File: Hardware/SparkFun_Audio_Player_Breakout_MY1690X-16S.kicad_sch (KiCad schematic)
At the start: 42 parts, among them J1 3.5mm TRRS, J2 Conn_01x03, J3 Conn_01x02, J4 USB_C_Receptacle, J5 Conn_01x06, J6 microSD, Q1 BSS138, U2 MY1690X-16S

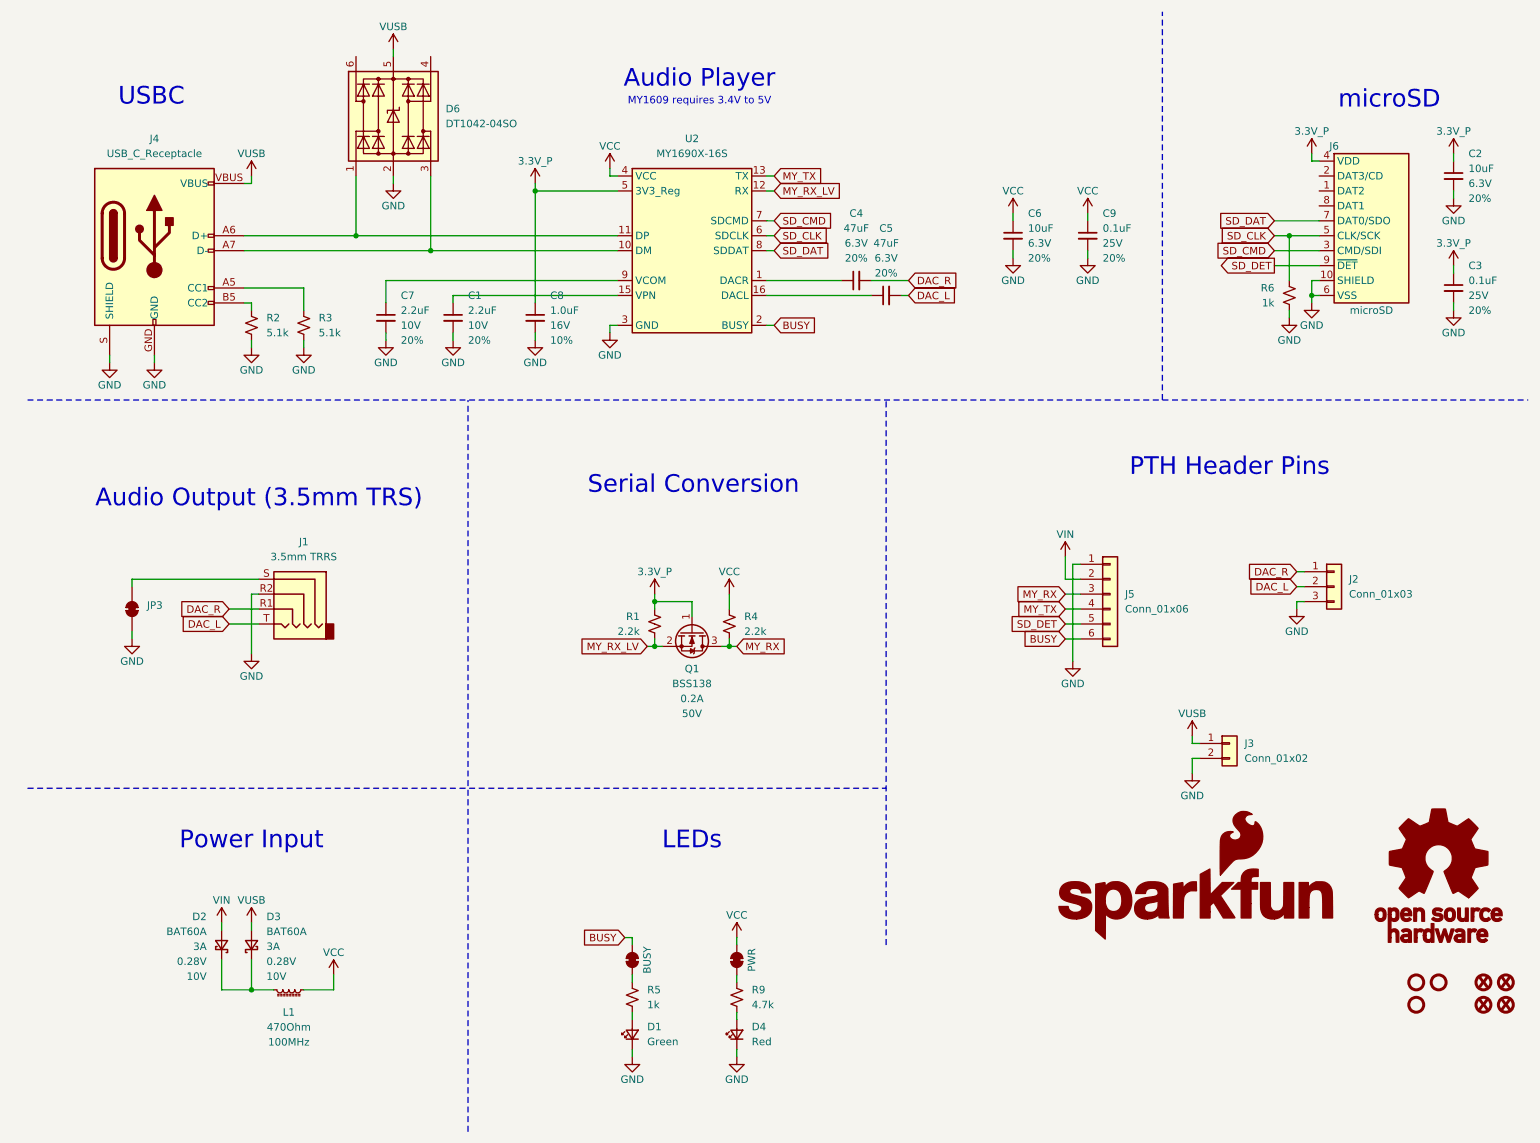
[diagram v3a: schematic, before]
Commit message: review changes 1
-TX bottom silk fishtail (output)
-centered position of OSHW logo
-nudged vcc vias near VUSB pth headers for better ground flow pour
-named JP3 "SLV"
-added jumper comments to sch
-moved C1/C8 to avoid text overlap in SCH
-added RD to jumpers in sch
-added NC flags to unused pins on SCH
-measures
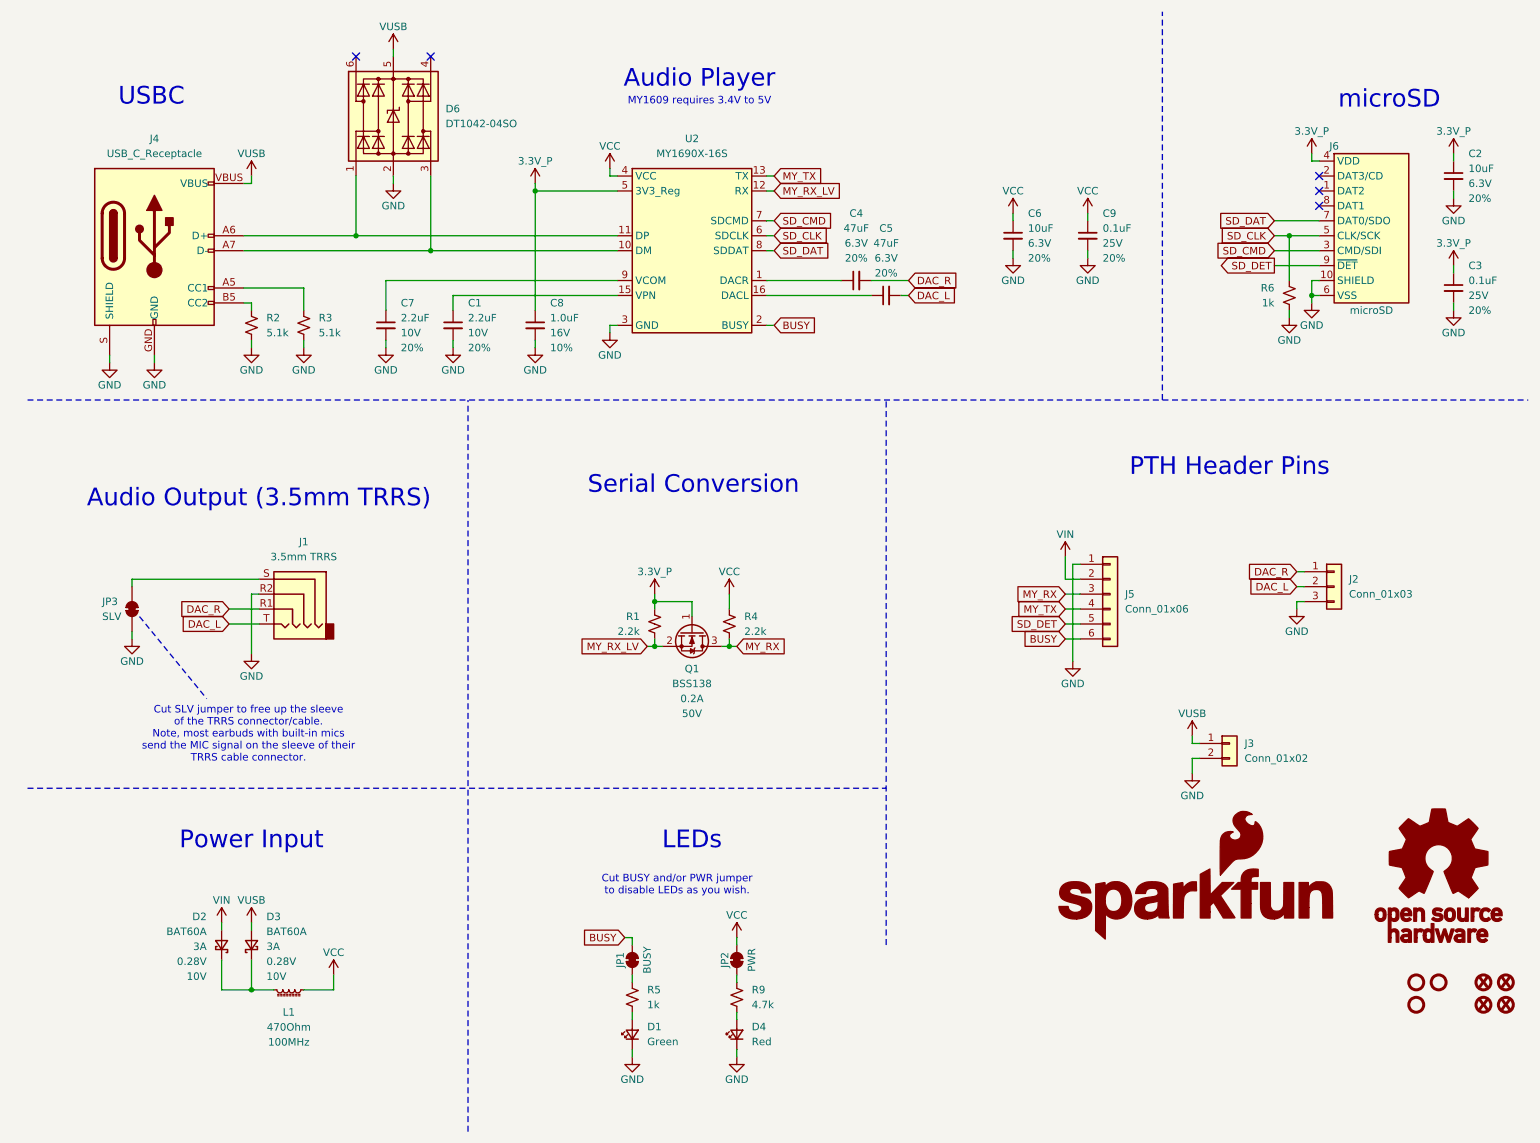
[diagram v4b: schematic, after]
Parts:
- JP3: value ~ -> SLV
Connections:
- no-connect marks 0 -> 5
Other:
- note added: "Audio Output (3.5mm TRRS)"
- note added: "Cut BUSY and/or PWR jumper to disable LEDs as you wish."
- note added: "Cut SLV jumper to free up the sleeve of the TRRS connector/cable. Note, most earbuds with built-in mics send the MIC signal on the sleeve of their TRRS cable connector."
- note removed: "Audio Output (3.5mm TRS)"
- moved on the sheet: C1, C7, C8
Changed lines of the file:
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@@
 		(color 0 0 0 0)
 	)
+	(no_connect
+		(at 81.28 20.32)
+	)
+	(no_connect
+		(at 232.41 40.64)
+	)
+	(no_connect
+		(at 68.58 20.32)
+	)
+	(no_connect
+		(at 232.41 43.18)
+	)
+	(no_connect
+		(at 232.41 45.72)
+	)
 	(wire
 		(pts
@@
 	(wire
 		(pts
-			(xy 73.66 68.58) (xy 73.66 67.31)
+			(xy 73.66 69.85) (xy 73.66 68.58)
 		)
 		(stroke
@@
 	(wire
 		(pts
-			(xy 85.09 60.96) (xy 85.09 62.23)
+			(xy 85.09 60.96) (xy 85.09 63.5)
 		)
 		(stroke
@@
 	(wire
 		(pts
-			(xy 73.66 58.42) (xy 73.66 62.23)
+			(xy 73.66 58.42) (xy 73.66 63.5)
 		)
 		(stroke
@@
 	(polyline
 		(pts
+			(xy 31.75 115.57) (xy 43.18 129.54)
+		)
+		(stroke
+			(width 0)
+			(type dash)
+			(color 132 132 132 1)
+		)
+	)
+	(polyline
+		(pts
 			(xy 12.7 78.74) (xy 137.16 78.74)
 		)
@@
 	(wire
 		(pts
-			(xy 99.06 43.18) (xy 99.06 62.23)
+			(xy 99.06 43.18) (xy 99.06 63.5)
 		)
 		(stroke
@@
 	(wire
 		(pts
-			(xy 85.09 68.58) (xy 85.09 67.31)
+			(xy 85.09 69.85) (xy 85.09 68.58)
 		)
 		(stroke
@@
 	(wire
 		(pts
-			(xy 99.06 68.58) (xy 99.06 67.31)
+			(xy 99.06 69.85) (xy 99.06 68.58)
 		)
 		(stroke
@@
 			(font
 				(size 1.27 1.27)
+				(color 132 132 132 1)
 			)
 		)
@@
 		)
 	)
-	(text "Audio Output (3.5mm TRS)"
+	(text "Audio Output (3.5mm TRRS)"
 		(exclude_from_sim no)
 		(at 52.07 95.504 0)
@@
 		)
 	)
+	(text "Cut BUSY and/or PWR jumper\nto disable LEDs as you wish."
+		(exclude_from_sim no)
+		(at 123.19 161.29 0)
+		(effects
+			(font
+				(size 1.27 1.27)
+				(color 132 132 132 1)
+			)
+		)
+	)
 	(text "USBC"
 		(exclude_from_sim no)
@@
 		)
 	)
+	(text "Cut SLV jumper to free up the sleeve\nof the TRRS connector/cable.\nNote, most earbuds with built-in mics\nsend the MIC signal on the sleeve of their\nTRRS cable connector."
+		(exclude_from_sim no)
+		(at 50.292 135.636 0)
+		(effects
+			(font
+				(size 1.27 1.27)
+				(color 132 132 132 1)
+			)
+		)
+	)
 	(text "Power Input"
 		(exclude_from_sim no)
@@
 	(symbol
 		(lib_id "SparkFun-Capacitor:2.2uF_0603_10V_20%")
-		(at 73.66 64.77 0)
+		(at 73.66 66.04 0)
 		(unit 1)
 		(exclude_from_sim no)
@@
 		(fields_autoplaced yes)
 		(property "Reference" "C7"
-			(at 76.2 60.9662 0)
+			(at 76.2 62.2362 0)
 			(effects
 				(font
@@
 		)
 		(property "Value" "2.2uF"
-			(at 76.2 63.5062 0)
+			(at 76.2 64.7762 0)
 			(effects
 				(font
@@
 		)
 		(property "Footprint" "SparkFun-Capacitor:C_0603_1608Metric"
-			(at 73.66 76.2 0)
+			(at 73.66 77.47 0)
 			(effects
 				(font
@@
 		)
 		(property "Datasheet" "https://cdn.sparkfun.com/assets/8/a/4/a/5/Kemet_Capacitor_Datasheet.pdf"
-			(at 74.93 81.28 0)
+			(at 74.93 82.55 0)
 			(effects
 				(font
@@
 		)
 		(property "Description" "Unpolarized capacitor"
-			(at 73.66 83.82 0)
+			(at 73.66 85.09 0)
 			(effects
 				(font
@@
 		)
 		(property "PROD_ID" "CAP-07888"
-			(at 72.39 78.74 0)
+			(at 72.39 80.01 0)
 			(effects
 				(font
@@
 		)
 		(property "Voltage" "10V"
-			(at 76.2 66.0462 0)
+			(at 76.2 67.3162 0)
 			(effects
 				(font
@@
 		)
 		(property "Tolerance" "20%"
-			(at 76.2 68.5862 0)
+			(at 76.2 69.8562 0)
 			(effects
 				(font
@@
 		(on_board yes)
 		(dnp no)
-		(fields_autoplaced yes)
 		(property "Reference" "JP3"
-			(at 33.02 113.6649 90)
+			(at 25.4 113.03 90)
 			(effects
 				(font
@@
 			)
 		)
-		(property "Value" "~"
-			(at 33.02 115.57 90)
+		(property "Value" "SLV"
+			(at 25.4 115.57 90)
 			(effects
 				(font
@@
 	(symbol
 		(lib_id "SparkFun-Capacitor:2.2uF_0603_10V_20%")
-		(at 85.09 64.77 0)
+		(at 85.09 66.04 0)
 		(unit 1)
 		(exclude_from_sim no)
@@
 		(fields_autoplaced yes)
 		(property "Reference" "C1"
-			(at 87.63 60.9662 0)
+			(at 87.63 62.2362 0)
 			(effects
 				(font
@@
 		)
 		(property "Value" "2.2uF"
-			(at 87.63 63.5062 0)
+			(at 87.63 64.7762 0)
 			(effects
 				(font
@@
 		)
 		(property "Footprint" "SparkFun-Capacitor:C_0603_1608Metric"
-			(at 85.09 76.2 0)
+			(at 85.09 77.47 0)
 			(effects
 				(font
@@
 		)
 		(property "Datasheet" "https://cdn.sparkfun.com/assets/8/a/4/a/5/Kemet_Capacitor_Datasheet.pdf"
-			(at 86.36 81.28 0)
+			(at 86.36 82.55 0)
 			(effects
 				(font
@@
 		)
 		(property "Description" "Unpolarized capacitor"
-			(at 85.09 83.82 0)
+			(at 85.09 85.09 0)
 			(effects
 				(font
@@
 		)
 		(property "PROD_ID" "CAP-07888"
-			(at 83.82 78.74 0)
+			(at 83.82 80.01 0)
 			(effects
 				(font
@@
 		)
 		(property "Voltage" "10V"
-			(at 87.63 66.0462 0)
+			(at 87.63 67.3162 0)
 			(effects
 				(font
@@
 		)
 		(property "Tolerance" "20%"
-			(at 87.63 68.5862 0)
+			(at 87.63 69.8562 0)
 			(effects
 				(font
@@
 	(symbol
 		(lib_id "SparkFun-Capacitor:1.0uF_0603_16V_10%")
-		(at 99.06 64.77 0)
+		(at 99.06 66.04 0)
 		(unit 1)
 		(exclude_from_sim no)
@@
 		(fields_autoplaced yes)
 		(property "Reference" "C8"
-			(at 101.6 60.9662 0)
+			(at 101.6 62.2362 0)
 			(effects
 				(font
@@
 		)
 		(property "Value" "1.0uF"
-			(at 101.6 63.5062 0)
+			(at 101.6 64.7762 0)
 			(effects
 				(font
@@
 		)
 		(property "Footprint" "SparkFun-Capacitor:C_0603_1608Metric"
-			(at 99.06 76.2 0)
+			(at 99.06 77.47 0)
 			(effects
 				(font
@@
 		)
 		(property "Datasheet" "https://cdn.sparkfun.com/assets/8/a/4/a/5/Kemet_Capacitor_Datasheet.pdf"
-			(at 99.06 78.74 0)
+			(at 99.06 80.01 0)
 			(effects
 				(font
@@
 		)
 		(property "Description" "Unpolarized capacitor"
-			(at 99.06 83.82 0)
+			(at 99.06 85.09 0)
 			(effects
 				(font
@@
 		)
 		(property "PROD_ID" "CAP-13930"
-			(at 97.79 81.28 0)
+			(at 97.79 82.55 0)
 			(effects
 				(font
@@
 		)
 		(property "Voltage" "16V"
-			(at 101.6 66.0462 0)
+			(at 101.6 67.3162 0)
 			(effects
 				(font
@@
 		)
 		(property "Tolerance" "10%"
-			(at 101.6 68.5862 0)
+			(at 101.6 69.8562 0)
 			(effects
 				(font
@@
 	(symbol
 		(lib_id "SparkFun-PowerSymbol:GND")
-		(at 85.09 68.58 0)
+		(at 85.09 69.85 0)
 		(unit 1)
 		(exclude_from_sim no)
@@
 		(dnp no)
 		(property "Reference" "#PWR013"
-			(at 85.09 74.93 0)
+			(at 85.09 76.2 0)
 			(effects
 				(font
@@
 		)
 		(property "Value" "GND"
-			(at 85.09 72.39 0)
+			(at 85.09 73.66 0)
 			(effects
 				(font
@@
 		)
 		(property "Footprint" ""
-			(at 85.09 68.58 0)
+			(at 85.09 69.85 0)
 			(effects
 				(font
@@
 		)
 		(property "Datasheet" ""
-			(at 85.09 68.58 0)
+			(at 85.09 69.85 0)
 			(effects
 				(font
@@
 		)
 		(property "Description" "Power symbol creates a global label with name \"GND\" , ground"
-			(at 85.09 68.58 0)
+			(at 85.09 69.85 0)
 			(effects
 				(font
@@
 	(symbol
 		(lib_id "SparkFun-PowerSymbol:GND")
-		(at 99.06 68.58 0)
+		(at 99.06 69.85 0)
 		(unit 1)
 		(exclude_from_sim no)
@@
 		(dnp no)
 		(property "Reference" "#PWR015"
-			(at 99.06 74.93 0)
+			(at 99.06 76.2 0)
 			(effects
 				(font
@@
 		)
 		(property "Value" "GND"
-			(at 99.06 72.39 0)
+			(at 99.06 73.66 0)
 			(effects
 				(font
@@
 		)
 		(property "Footprint" ""
-			(at 99.06 68.58 0)
+			(at 99.06 69.85 0)
 			(effects
 				(font
@@
 		)
 		(property "Datasheet" ""
-			(at 99.06 68.58 0)
+			(at 99.06 69.85 0)
 			(effects
 				(font
@@
 		)
 		(property "Description" "Power symbol creates a global label with name \"GND\" , ground"
-			(at 99.06 68.58 0)
+			(at 99.06 69.85 0)
 			(effects
 				(font
@@
 	(symbol
 		(lib_id "SparkFun-PowerSymbol:GND")
-		(at 73.66 68.58 0)
+		(at 73.66 69.85 0)
 		(unit 1)
 		(exclude_from_sim no)
@@
 		(dnp no)
 		(property "Reference" "#PWR014"
-			(at 73.66 74.93 0)
+			(at 73.66 76.2 0)
 			(effects
 				(font
@@
 		)
 		(property "Value" "GND"
-			(at 73.66 72.39 0)
+			(at 73.66 73.66 0)
 			(effects
 				(font
@@
 		)
 		(property "Footprint" ""
-			(at 73.66 68.58 0)
+			(at 73.66 69.85 0)
 			(effects
 				(font
@@
 		)
 		(property "Datasheet" ""
-			(at 73.66 68.58 0)
+			(at 73.66 69.85 0)
 			(effects
 				(font
@@
 		)
 		(property "Description" "Power symbol creates a global label with name \"GND\" , ground"
-			(at 73.66 68.58 0)
+			(at 73.66 69.85 0)
 			(effects
 				(font
@@
 					(size 1.27 1.27)
 				)
-				(hide yes)
 			)
 		)
@@
 					(size 1.27 1.27)
 				)
-				(hide yes)
 			)
 		)

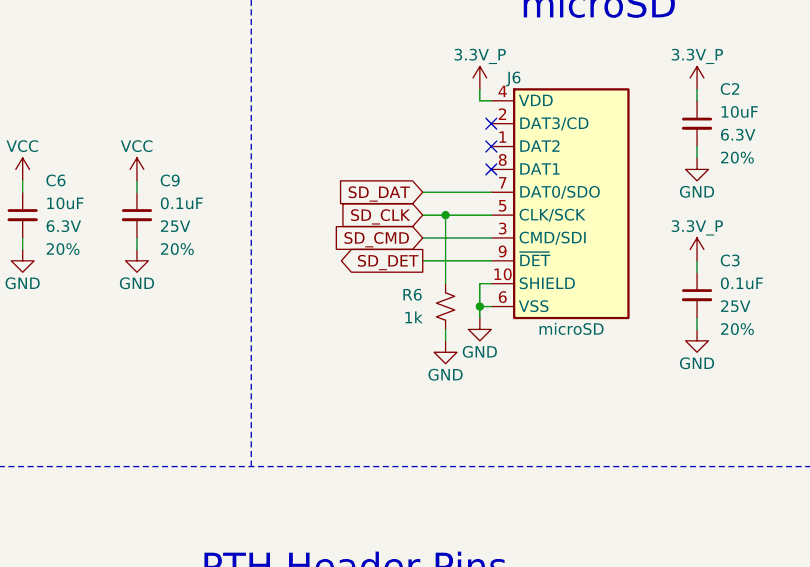
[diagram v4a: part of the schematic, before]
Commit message: removed R6 pull-down on uSD CLK line
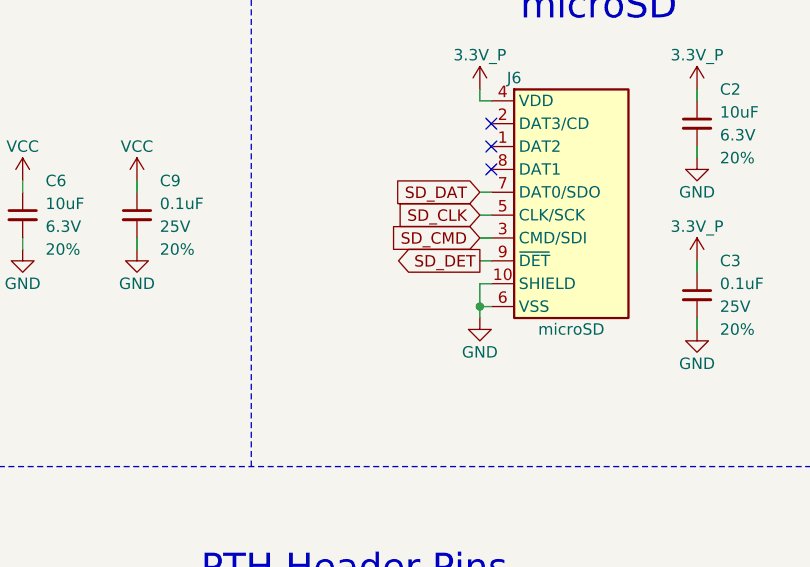
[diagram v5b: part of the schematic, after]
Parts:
- removed R6: 1k, SparkFun-Resistor:R_0603_1608Metric, symbol SparkFun-Resistor:1k_0603
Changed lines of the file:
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@@
 	)
 	(junction
-		(at 227.33 50.8)
-		(diameter 0)
-		(color 0 0 0 0)
-	)
-	(junction
 		(at 81.28 53.34)
 		(diameter 0)
@@
 	(wire
 		(pts
-			(xy 224.79 48.26) (xy 232.41 48.26)
+			(xy 231.14 48.26) (xy 232.41 48.26)
 		)
 		(stroke
@@
 	(wire
 		(pts
-			(xy 224.79 53.34) (xy 232.41 53.34)
+			(xy 231.14 53.34) (xy 232.41 53.34)
 		)
 		(stroke
@@
 	(wire
 		(pts
-			(xy 224.79 50.8) (xy 227.33 50.8)
-		)
-		(stroke
-			(width 0)
-			(type default)
-		)
-	)
-	(wire
-		(pts
-			(xy 227.33 50.8) (xy 232.41 50.8)
+			(xy 231.14 50.8) (xy 232.41 50.8)
 		)
 		(stroke
@@
 	(wire
 		(pts
-			(xy 224.79 55.88) (xy 232.41 55.88)
+			(xy 231.14 55.88) (xy 232.41 55.88)
 		)
 		(stroke
@@
 	(wire
 		(pts
-			(xy 227.33 50.8) (xy 227.33 58.42)
-		)
-		(stroke
-			(width 0)
-			(type default)
-		)
-	)
-	(wire
-		(pts
 			(xy 49.53 62.23) (xy 50.8 62.23)
 		)
@@
 	(wire
 		(pts
-			(xy 227.33 64.77) (xy 227.33 63.5)
-		)
-		(stroke
-			(width 0)
-			(type default)
-		)
-	)
-	(wire
-		(pts
 			(xy 138.43 60.96) (xy 156.21 60.96)
 		)
@@
 	(global_label "SD_DAT"
 		(shape input)
-		(at 224.79 48.26 180)
+		(at 231.14 48.26 180)
 		(fields_autoplaced yes)
 		(effects
@@
 		)
 		(property "Intersheetrefs" "${INTERSHEET_REFS}"
-			(at 215.0315 48.26 0)
+			(at 221.3815 48.26 0)
 			(effects
 				(font
@@
 	(global_label "SD_DET"
 		(shape output)
-		(at 224.79 55.88 180)
+		(at 231.14 55.88 180)
 		(fields_autoplaced yes)
 		(effects
@@
 		)
 		(property "Intersheetrefs" "${INTERSHEET_REFS}"
-			(at 214.9711 55.88 0)
+			(at 221.3211 55.88 0)
 			(effects
 				(font
@@
 	(global_label "SD_CMD"
 		(shape input)
-		(at 224.79 53.34 180)
+		(at 231.14 53.34 180)
 		(fields_autoplaced yes)
 		(effects
@@
 		)
 		(property "Intersheetrefs" "${INTERSHEET_REFS}"
-			(at 214.3663 53.34 0)
+			(at 220.7163 53.34 0)
 			(effects
 				(font
@@
 	(global_label "SD_CLK"
 		(shape input)
-		(at 224.79 50.8 180)
+		(at 231.14 50.8 180)
 		(fields_autoplaced yes)
 		(effects
@@
 		)
 		(property "Intersheetrefs" "${INTERSHEET_REFS}"
-			(at 214.7896 50.8 0)
+			(at 221.1396 50.8 0)
 			(effects
 				(font
@@
 	)
 	(symbol
-		(lib_id "SparkFun-Resistor:1k_0603")
-		(at 227.33 60.96 90)
-		(unit 1)
-		(exclude_from_sim no)
-		(in_bom yes)
-		(on_board yes)
-		(dnp no)
-		(fields_autoplaced yes)
-		(property "Reference" "R6"
-			(at 224.79 59.6899 90)
-			(effects
-				(font
-					(size 1.27 1.27)
-				)
-				(justify left)
-			)
-		)
-		(property "Value" "1k"
-			(at 224.79 62.2299 90)
-			(effects
-				(font
-					(size 1.27 1.27)
-				)
-				(justify left)
-			)
-		)
-		(property "Footprint" "SparkFun-Resistor:R_0603_1608Metric"
-			(at 231.902 60.96 0)
-			(effects
-				(font
-					(size 1.27 1.27)
-				)
-				(hide yes)
-			)
-		)
-		(property "Datasheet" "https://www.vishay.com/docs/20035/dcrcwe3.pdf"
-			(at 236.22 62.23 0)
-			(effects
-				(font
-					(size 1.27 1.27)
-				)
-				(hide yes)
-			)
-		)
-		(property "Description" "Resistor"
-			(at 238.76 60.96 0)
-			(effects
-				(font
-					(size 1.27 1.27)
-				)
-				(hide yes)
-			)
-		)
-		(property "PROD_ID" "RES-07856"
-			(at 234.188 60.96 0)
-			(effects
-				(font
-					(size 1.27 1.27)
-				)
-				(hide yes)
-			)
-		)
-		(pin "2"
-		)
-		(pin "1"
-		)
-		(instances
-			(project ""
-				(path "/e3dd3ae4-244d-4cba-9cca-5d2abf83f29a"
-					(reference "R6")
-					(unit 1)
-				)
-			)
-		)
-	)
-	(symbol
 		(lib_id "SparkFun-Hardware:Standoff")
 		(at 248.92 181.61 0)
@@
 					(unit 1)
 				)
-			)
-		)
-	)
-	(symbol
-		(lib_id "SparkFun-PowerSymbol:GND")
-		(at 227.33 64.77 0)
-		(unit 1)
-		(exclude_from_sim no)
-		(in_bom yes)
-		(on_board yes)
-		(dnp no)
-		(property "Reference" "#PWR019"
-			(at 227.33 71.12 0)
-			(effects
-				(font
-					(size 1.27 1.27)
-				)
-				(hide yes)
-			)
-		)
-		(property "Value" "GND"
-			(at 227.33 68.58 0)
-			(effects
-				(font
-					(size 1.27 1.27)
-				)
-			)
-		)
-		(property "Footprint" ""
-			(at 227.33 64.77 0)
-			(effects
-				(font
-					(size 1.27 1.27)
-				)
-				(hide yes)
-			)
-		)
-		(property "Datasheet" ""
-			(at 227.33 64.77 0)
-			(effects
-				(font
-					(size 1.27 1.27)
-				)
-				(hide yes)
-			)
-		)
-		(property "Description" "Power symbol creates a global label with name \"GND\" , ground"
-			(at 227.33 64.77 0)
-			(effects
-				(font
-					(size 1.27 1.27)
-				)
-				(hide yes)
-			)
-		)
-		(pin "1"
-		)
-		(instances
-			(project "SparkFun_MP3_Serial_MY1690X_Breakout"
-				(path "/e3dd3ae4-244d-4cba-9cca-5d2abf83f29a"
-					(reference "#PWR019")
-					(unit 1)
-				)
